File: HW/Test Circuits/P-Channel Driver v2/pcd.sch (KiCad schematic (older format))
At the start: 21 parts, among them J1 PWR, J2 PWM_IN, J3 OUT, Q1 2N7000, Q2 2N3019, Q3 2N7000, Q4 IRF9530

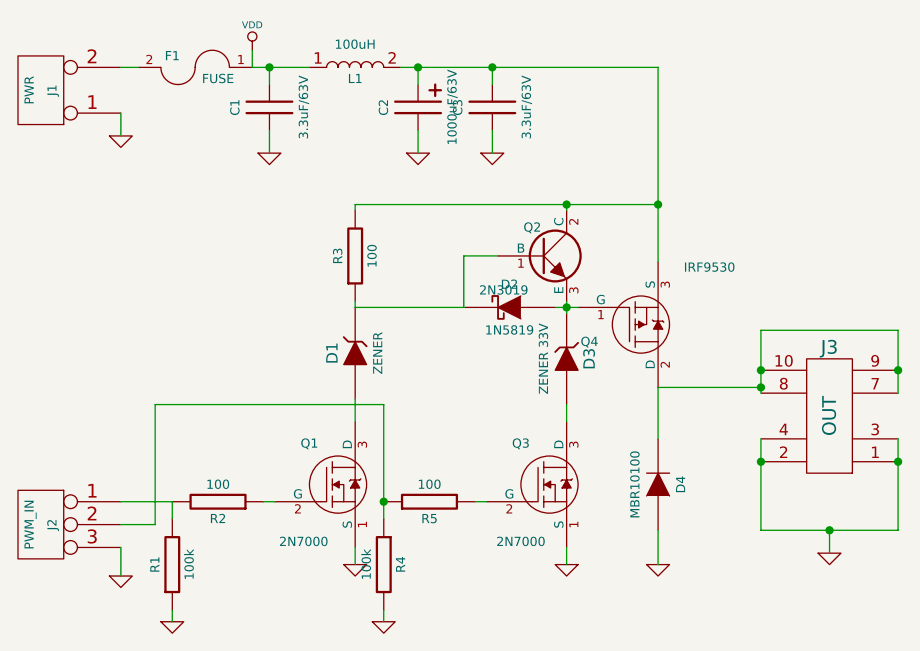
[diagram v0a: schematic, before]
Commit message: Motor Measurement V2 added
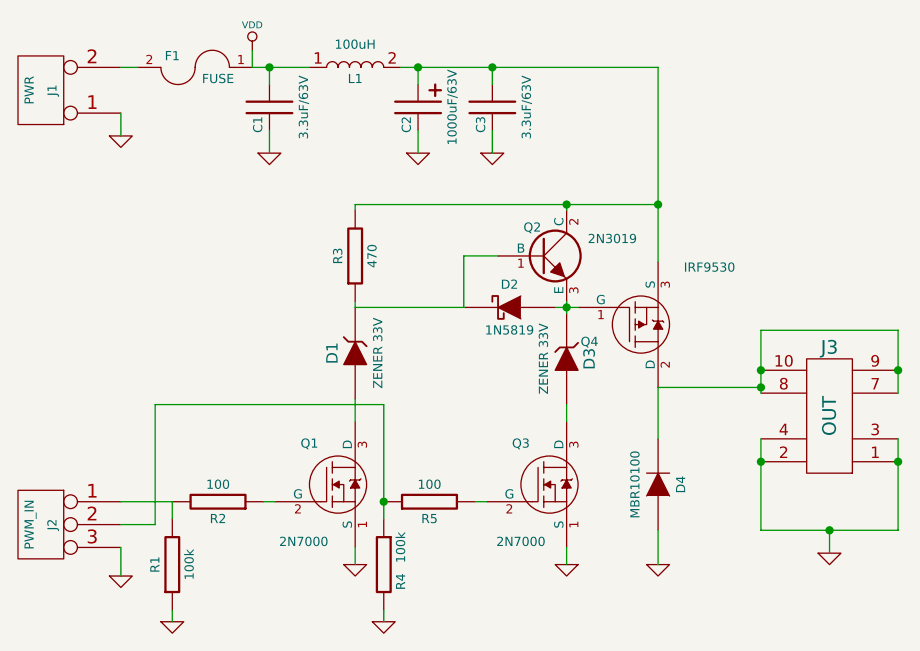
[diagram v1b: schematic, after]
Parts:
- D1: value ZENER -> ZENER 33V
- R3: value 100 -> 470
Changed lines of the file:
@@
 Sheet 1 1
 Title ""
-Date "21 apr 2015"
+Date "24 apr 2015"
 Rev ""
 Comp ""
@@
 P 3000 1625
 F 0 "Q2" H 2950 1750 40  0000 C CNN
-F 1 "2N3019" H 2825 1475 40  0000 C CNN
+F 1 "2N3019" H 3300 1700 40  0000 C CNN
 F 2 "TO-39" H 3000 1625 60  0001 C CNN
 F 3 "~" H 3000 1625 60  0000 C CNN
@@
 U 1 1 552FDD09
 P 2450 975
-F 0 "C2" H 2450 825 40  0000 C CNN
+F 0 "C2" H 2525 925 40  0000 C CNN
 F 1 "1000uF/63V" H 2450 1125 40  0000 C CNN
 F 2 "C3P_D7" H 2450 975 60  0001 C CNN
@@
 U 1 1 552FDD27
 P 2775 975
-F 0 "C3" H 2775 825 40  0000 C CNN
+F 0 "C3" H 2850 925 40  0000 C CNN
 F 1 "3.3uF/63V" H 2775 1125 40  0000 C CNN
 F 2 "C2_3x3" H 2775 975 60  0001 C CNN
@@
 U 1 1 552FDD36
 P 1800 975
-F 0 "C1" H 1800 825 40  0000 C CNN
+F 0 "C1" H 1875 925 40  0000 C CNN
 F 1 "3.3uF/63V" H 1800 1125 40  0000 C CNN
 F 2 "C2_3x3" H 1800 975 60  0001 C CNN
@@
 P 2175 2050
 F 0 "D1" H 2175 2150 50  0000 C CNN
-F 1 "ZENER" H 2175 1950 40  0000 C CNN
+F 1 "ZENER 33V" H 2175 1950 40  0000 C CNN
 F 2 "D3" H 2175 2050 60  0001 C CNN
 F 3 "" H 2175 2050 60  0000 C CNN
@@
 P 2175 1625
 F 0 "R3" H 2175 1550 40  0000 C CNN
-F 1 "100" H 2175 1700 40  0000 C CNN
+F 1 "470" H 2175 1700 40  0000 C CNN
 F 2 "R4" H 2175 1625 60  0001 C CNN
 F 3 "~" H 2175 1625 60  0000 C CNN
@@
 U 1 1 55356B1C
 P 2300 2975
-F 0 "R4" H 2300 2900 40  0000 C CNN
-F 1 "100k" H 2300 3050 40  0000 C CNN
+F 0 "R4" H 2225 2900 40  0000 C CNN
+F 1 "100k" H 2375 2900 40  0000 C CNN
 F 2 "R4" H 2300 2975 60  0001 C CNN
 F 3 "~" H 2300 2975 60  0000 C CNN
